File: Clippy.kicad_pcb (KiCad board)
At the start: 2 copper layers, 61.2 x 38.4 mm, 15 parts, among them J1 Conn_01x08, SW1 PEC11R-4215F-S0024, U1 tiny2040, U2 SN74LV1T34DBV

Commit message: Final touches?
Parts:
- added C2: 100nF, Capacitor_SMD:C_0402_1005Metric_Pad0.74x0.62mm_HandSolder, B.Cu at (150.3, 92.5)
- added C3: 100nF, Capacitor_SMD:C_0402_1005Metric_Pad0.74x0.62mm_HandSolder, B.Cu at (169.3, 92.4)
- moved D1 1.27 mm to (127.5, 83.7)
- moved D2 1.27 mm to (131.3, 83.7)
- moved D3 1.27 mm to (135.1, 83.7)
- moved D4 1.27 mm to (138.9, 83.7)
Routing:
- net +5V: track 124.9 -> 126.2 mm
- net Net-(D2-A): track 29.9 -> 30.4 mm
- net Net-(D3-A): track 49.7 -> 50.2 mm
- net Net-(D1-A): track 58.4 -> 58.9 mm
- net ROW1: track 19.6 -> 19.1 mm
- net Net-(D4-A): track 35.8 -> 36.4 mm
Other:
- board text added: "+3V3"
- board text added: "+5V"
- board text added: "GND"
- board text added: "GP26"
- board text added: "GP27"
- board text added: "GP28"
- board text added: "GP29"
- board text added: "GP7"

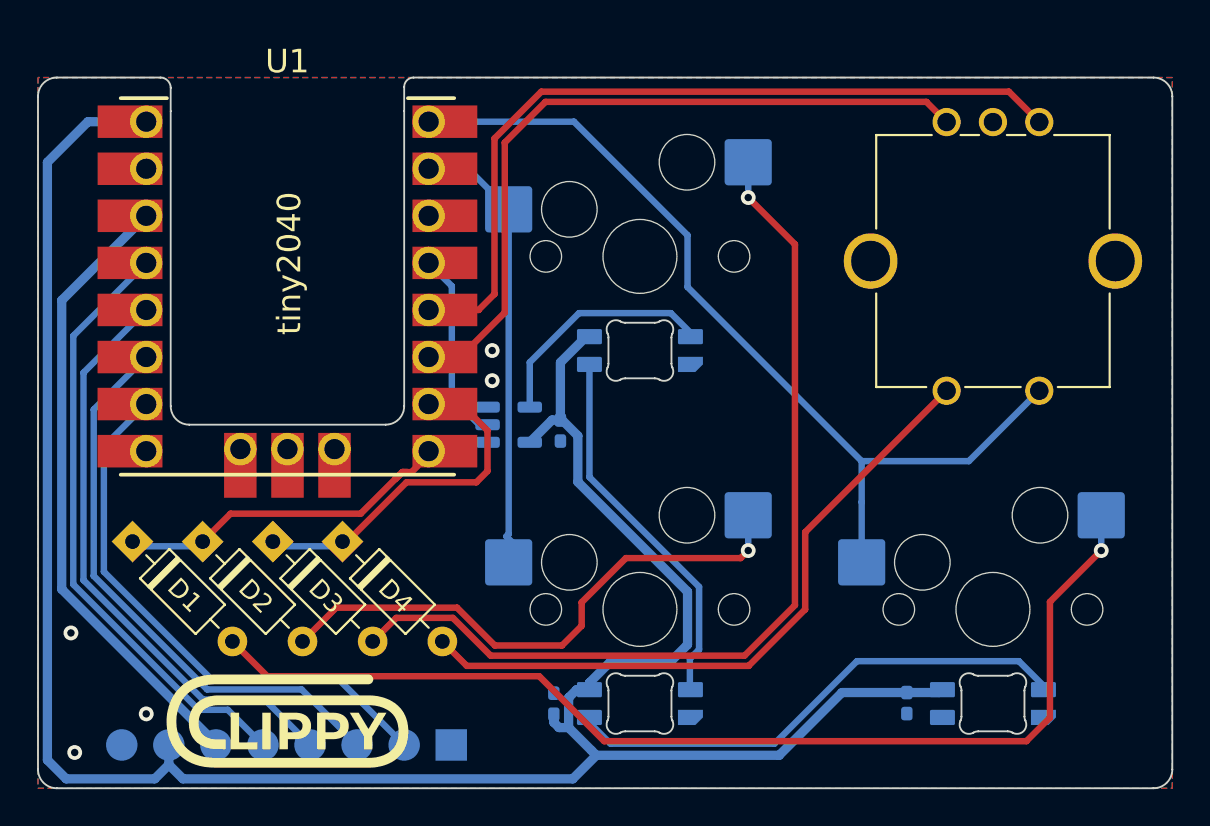
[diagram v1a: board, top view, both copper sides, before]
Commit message: oops. Actually add tooling holes
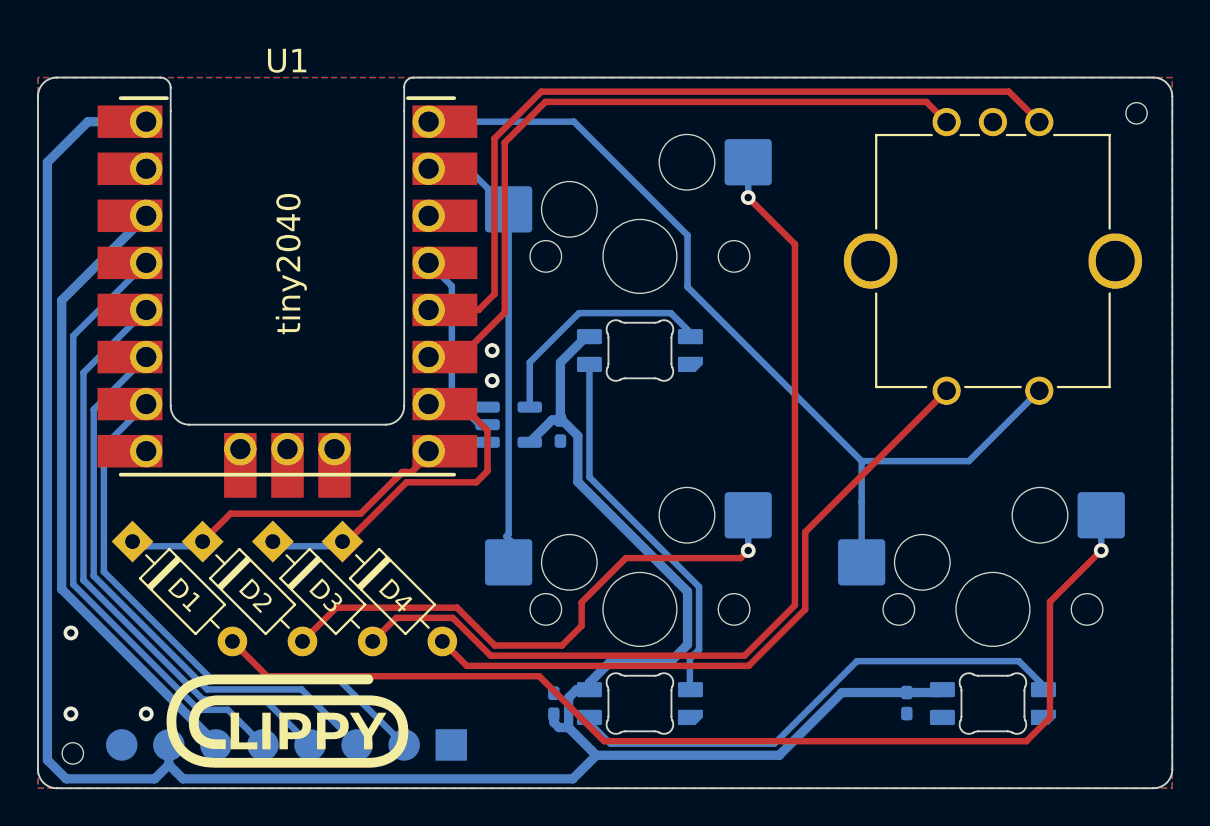
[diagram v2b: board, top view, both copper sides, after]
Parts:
- added REF**: MountingHole_1.152mm, MountingHole:MountingHole_1.152mm, F.Cu at (181.7, 60.6)
- added REF**: MountingHole_1.152mm, MountingHole:MountingHole_1.152mm, F.Cu at (124.3, 95.1)
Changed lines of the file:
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@@
       (net 5 "Net-(D3-A)") (pinfunction "ROW") (pintype "passive"))
+  )
+  (footprint "MountingHole:MountingHole_1.152mm" (layer "F.Cu")
+    (at 181.7116 60.6044)
+    (descr "Mounting Hole 2.1mm, no annular")
+    (tags "mounting hole 2.1mm no annular")
+    (attr exclude_from_pos_files exclude_from_bom)
+    (fp_text reference "REF**" (at 0 -3.2) (layer "F.SilkS") hide
+        (effects (font (size 1 1) (thickness 0.15)))
+    )
+    (fp_text value "MountingHole_1.152mm" (at 0 3.2) (layer "F.Fab")
+        (effects (font (size 1 1) (thickness 0.15)))
+    )
+    (fp_text user "${REFERENCE}" (at 0 0) (layer "F.Fab")
+        (effects (font (size 1 1) (thickness 0.15)))
+    )
+    (fp_circle (center 0 0) (end 1.25 0)
+      (stroke (width 0.15) (type solid)) (fill none) (layer "Cmts.User"))
+    (fp_circle (center 0 0) (end 1.5 0)
+      (stroke (width 0.05) (type solid)) (fill none) (layer "F.CrtYd"))
+    (pad "" np_thru_hole circle (at 0 0) (size 1.152 1.152) (drill 1.152) (layers "F&B.Cu" "*.Mask")
+      (solder_mask_margin 0.148))
   )
   (footprint "Diode_THT:D_DO-35_SOD27_P7.62mm_Horizontal" (layer "F.Cu")
@@
       (rotate (xyz 0 0 0))
     )
+  )
+  (footprint "MountingHole:MountingHole_1.152mm" (layer "F.Cu")
+    (at 124.3076 95.1484)
+    (descr "Mounting Hole 2.1mm, no annular")
+    (tags "mounting hole 2.1mm no annular")
+    (attr exclude_from_pos_files exclude_from_bom)
+    (fp_text reference "REF**" (at 0 -3.2) (layer "F.SilkS") hide
+        (effects (font (size 1 1) (thickness 0.15)))
+    )
+    (fp_text value "MountingHole_1.152mm" (at 0 3.2) (layer "F.Fab")
+        (effects (font (size 1 1) (thickness 0.15)))
+    )
+    (fp_text user "${REFERENCE}" (at 0 0) (layer "F.Fab")
+        (effects (font (size 1 1) (thickness 0.15)))
+    )
+    (fp_circle (center 0 0) (end 1.25 0)
+      (stroke (width 0.15) (type solid)) (fill none) (layer "Cmts.User"))
+    (fp_circle (center 0 0) (end 1.5 0)
+      (stroke (width 0.05) (type solid)) (fill none) (layer "F.CrtYd"))
+    (pad "" np_thru_hole circle (at 0 0) (size 1.152 1.152) (drill 1.152) (layers "*.Cu" "*.Mask")
+      (solder_mask_margin 0.148))
   )
   (footprint "Rotary_Encoder:RotaryEncoder_Bourns_Vertical_PEC12R-3xxxF-Sxxxx" (layer "F.Cu")
@@
     (fp_arc (start -1.699999 0.702844) (mid -1.712527 0.814069) (end -1.749484 0.919721)
       (stroke (width 0.1) (type solid)) (layer "Edge.Cuts"))
-    (fp_arc (start -1.046711 1.568299) (mid -1.638071 1.504035) (end -1.749484 0.919721)
+    (fp_arc (start -1.046711 1.568299) (mid -1.63807 1.504035) (end -1.749484 0.919721)
       (stroke (width 0.1) (type solid)) (layer "Edge.Cuts"))
     (fp_arc (start -1.046711 1.568299) (mid -0.925123 1.517377) (end -0.794453 1.5)
@@
     (fp_arc (start 1.749484 0.919721) (mid 1.638072 1.504036) (end 1.046711 1.5683)
       (stroke (width 0.1) (type solid)) (layer "Edge.Cuts"))
-    (fp_arc (start 1.749484 0.919721) (mid 1.712539 0.814068) (end 1.699999 0.702843)
+    (fp_arc (start 1.749484 0.919721) (mid 1.712534 0.814067) (end 1.699999 0.702843)
       (stroke (width 0.1) (type solid)) (layer "Edge.Cuts"))
     (fp_line (start -3.8 -1.999999) (end -3.8 2.000001)
@@
     (fp_arc (start -1.699999 0.702844) (mid -1.712527 0.814069) (end -1.749484 0.919721)
       (stroke (width 0.1) (type solid)) (layer "Edge.Cuts"))
-    (fp_arc (start -1.046711 1.568299) (mid -1.638071 1.504035) (end -1.749484 0.919721)
+    (fp_arc (start -1.046711 1.568299) (mid -1.63807 1.504035) (end -1.749484 0.919721)
       (stroke (width 0.1) (type solid)) (layer "Edge.Cuts"))
     (fp_arc (start -1.046711 1.568299) (mid -0.925123 1.517377) (end -0.794453 1.5)
@@
     (fp_arc (start 1.749484 0.919721) (mid 1.638072 1.504036) (end 1.046711 1.5683)
       (stroke (width 0.1) (type solid)) (layer "Edge.Cuts"))
-    (fp_arc (start 1.749484 0.919721) (mid 1.712539 0.814068) (end 1.699999 0.702843)
+    (fp_arc (start 1.749484 0.919721) (mid 1.712534 0.814067) (end 1.699999 0.702843)
       (stroke (width 0.1) (type solid)) (layer "Edge.Cuts"))
     (fp_line (start -3.8 -1.999999) (end -3.8 2.000001)
@@
     (fp_arc (start -1.699999 0.702844) (mid -1.712527 0.814069) (end -1.749484 0.919721)
       (stroke (width 0.1) (type solid)) (layer "Edge.Cuts"))
-    (fp_arc (start -1.046711 1.568299) (mid -1.638071 1.504035) (end -1.749484 0.919721)
+    (fp_arc (start -1.046711 1.568299) (mid -1.63807 1.504035) (end -1.749484 0.919721)
       (stroke (width 0.1) (type solid)) (layer "Edge.Cuts"))
     (fp_arc (start -1.046711 1.568299) (mid -0.925123 1.517377) (end -0.794453 1.5)
@@
     (fp_arc (start 1.749484 0.919721) (mid 1.638072 1.504036) (end 1.046711 1.5683)
       (stroke (width 0.1) (type solid)) (layer "Edge.Cuts"))
-    (fp_arc (start 1.749484 0.919721) (mid 1.712539 0.814068) (end 1.699999 0.702843)
+    (fp_arc (start 1.749484 0.919721) (mid 1.712534 0.814067) (end 1.699999 0.702843)
       (stroke (width 0.1) (type solid)) (layer "Edge.Cuts"))
     (fp_line (start -3.8 -1.999999) (end -3.8 2.000001)
@@
   (via (at 146.939 73.406) (size 0.8) (drill 0.4) (layers "F.Cu" "B.Cu") (free) (net 12))
   (via (at 128.27 93.0148) (size 0.8) (drill 0.4) (layers "F.Cu" "B.Cu") (free) (net 12))
-  (via (at 124.4092 95.0976) (size 0.8) (drill 0.4) (layers "F.Cu" "B.Cu") (free) (net 12))
+  (via (at 124.206 93.0148) (size 0.8) (drill 0.4) (layers "F.Cu" "B.Cu") (free) (net 12))
   (via (at 124.206 88.646) (size 0.8) (drill 0.4) (layers "F.Cu" "B.Cu") (free) (net 12))
   (segment (start 175.365187 90.17) (end 166.624 90.17) (width 0.35) (layer "B.Cu") (net 13))

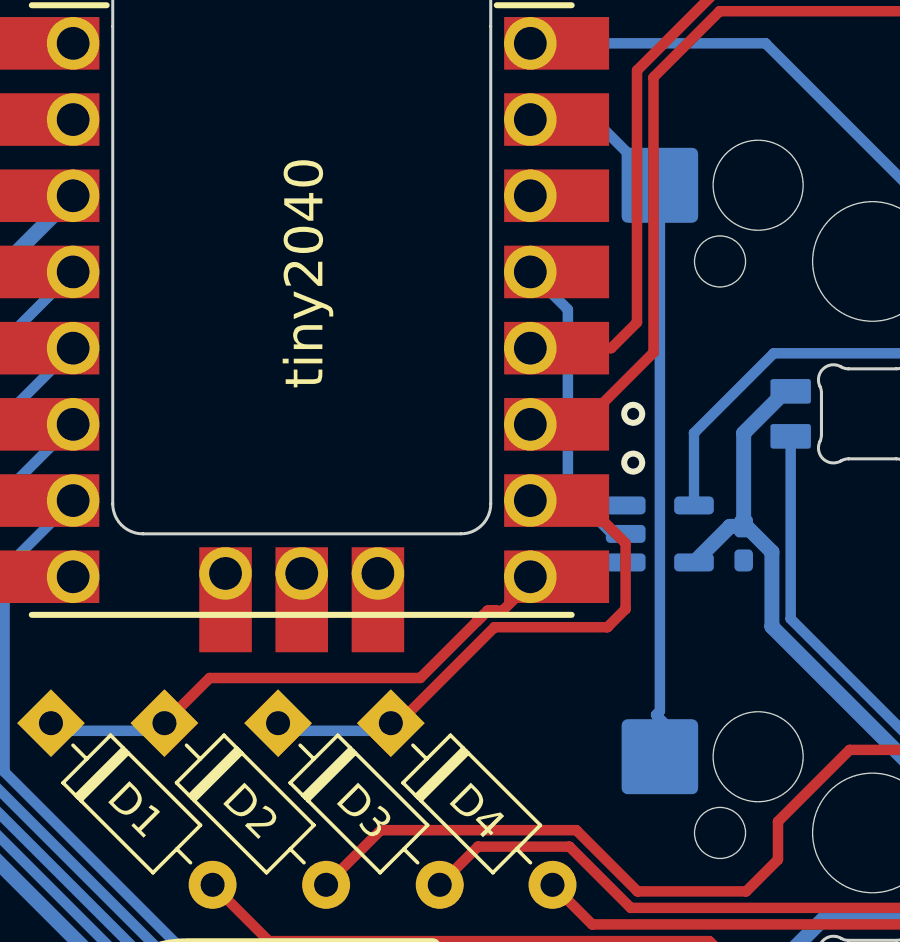
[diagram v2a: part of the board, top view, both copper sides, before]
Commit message: Fix DRC errors to a reasonable extent
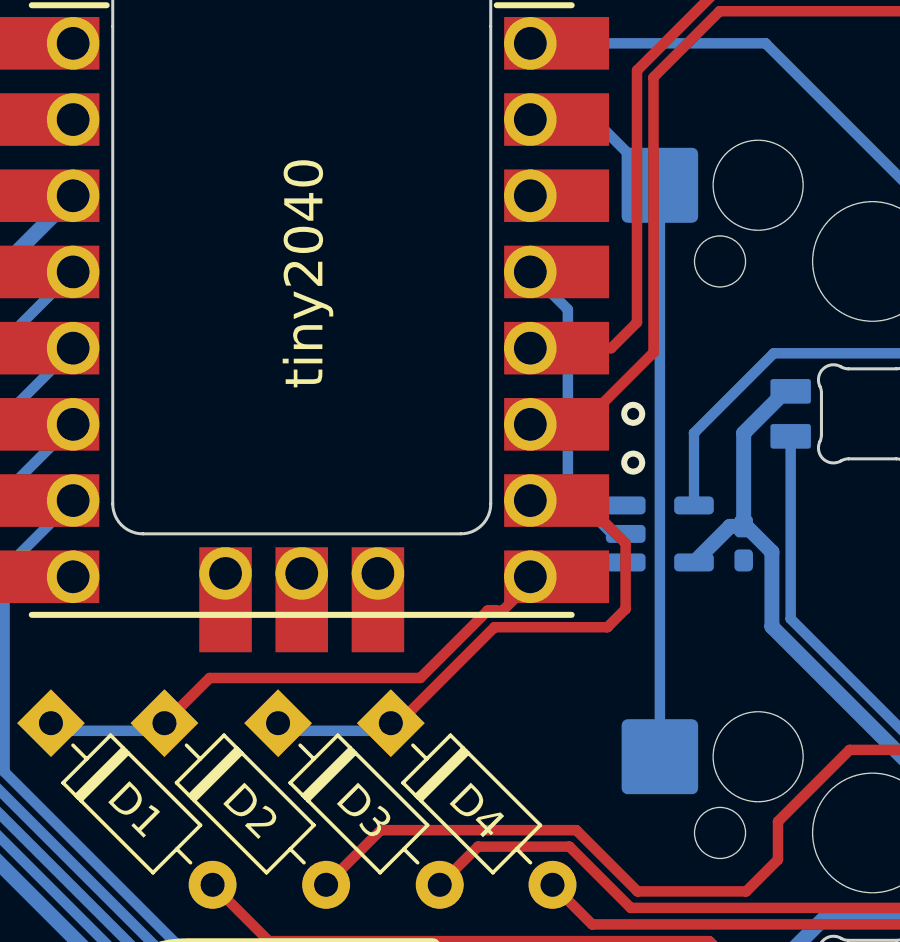
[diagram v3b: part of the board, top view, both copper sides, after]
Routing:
- net COL0: track 26.3 -> 24.3 mm
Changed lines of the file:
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@@
   )
   (segment (start 142.5868 79.968) (end 143.51 79.0448) (width 0.35) (layer "F.Cu") (net 1))
+  (segment (start 132.82018 82.210353) (end 139.843516 82.210353) (width 0.35) (layer "F.Cu") (net 1))
   (segment (start 143.51 79.0448) (end 143.51 78.83605) (width 0.35) (layer "F.Cu") (net 1))
+  (segment (start 139.843516 82.210353) (end 142.085869 79.968) (width 0.35) (layer "F.Cu") (net 1))
   (segment (start 142.092818 79.96105) (end 142.362488 79.96105) (width 0.35) (layer "F.Cu") (net 1))
-  (segment (start 139.843515 82.210353) (end 141.93335 80.120518) (width 0.35) (layer "F.Cu") (net 1))
-  (segment (start 132.82018 82.210353) (end 139.843515 82.210353) (width 0.35) (layer "F.Cu") (net 1))
-  (segment (start 141.710134 80.343734) (end 142.092818 79.96105) (width 0.35) (layer "F.Cu") (net 1))
+  (segment (start 131.313809 83.716724) (end 132.82018 82.210353) (width 0.35) (layer "F.Cu") (net 1))
   (segment (start 142.085869 79.968) (end 142.5868 79.968) (width 0.35) (layer "F.Cu") (net 1))
-  (segment (start 131.313809 83.716724) (end 132.82018 82.210353) (width 0.35) (layer "F.Cu") (net 1))
   (segment (start 127.530886 83.970724) (end 131.313809 83.970724) (width 0.35) (layer "B.Cu") (net 1))
   (segment (start 177.038 93.218) (end 175.768 94.488) (width 0.35) (layer "F.Cu") (net 2))
@@
   (segment (start 153.326 94.625) (end 152.188 93.487) (width 0.35) (layer "B.Cu") (net 13))
   (segment (start 152.188 93.487) (end 152.188 93.206) (width 0.35) (layer "B.Cu") (net 13))
-  (segment (start 147.828 84.836) (end 148.844 83.82) (width 0.35) (layer "B.Cu") (net 14))
-  (segment (start 148.463 84.201) (end 147.701 83.439) (width 0.35) (layer "B.Cu") (net 14))
-  (segment (start 147.828 83.312) (end 147.828 65.786) (width 0.35) (layer "B.Cu") (net 14))
-  (segment (start 147.701 83.439) (end 147.828 83.312) (width 0.35) (layer "B.Cu") (net 14))
   (segment (start 145.63805 63.59605) (end 143.51 63.59605) (width 0.35) (layer "B.Cu") (net 14))
-  (segment (start 147.828 84.836) (end 148.463 84.201) (width 0.35) (layer "B.Cu") (net 14))
   (segment (start 147.828 65.786) (end 145.63805 63.59605) (width 0.35) (layer "B.Cu") (net 14))
+  (segment (start 147.828 84.836) (end 147.828 65.786) (width 0.35) (layer "B.Cu") (net 14))
   (segment (start 143.51 61.05605) (end 151.35305 61.05605) (width 0.35) (layer "B.Cu") (net 15))
   (segment (start 166.878 79.375) (end 166.878 81.5848) (width 0.35) (layer "B.Cu") (net 15))

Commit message: finishing touches
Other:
- board text added: "Clippy Rev. 1 • April 2023"

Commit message: finishing touches 2 electric boogaloo
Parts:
- removed the REF** at (181.7, 60.6)
- removed the REF** at (124.3, 95.1)
- added REF**: MountingHole_1.152mm, MountingHole:MountingHole_1.152mm, F.Cu at (124.3, 95.1)
- added REF**: MountingHole_1.152mm, MountingHole:MountingHole_1.152mm, F.Cu at (181.7, 60.6)
- C1, C2, C3: footprint Capacitor_SMD:C_0402_1005Metric_Pad0.74x0.62mm_HandSolder -> Capacitor_SMD:C_0805_2012Metric_Pad1.18x1.45mm_HandSolder
- moved C1 1.42 mm to (151.9, 78.4), turned to 180 degrees
- moved C2 0.41 mm to (149.9, 92.5)
- moved C3 0.41 mm to (168.9, 92.4)
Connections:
- J1 pad 1: GP7 -> GP2
- U1 pad 14: unconnected-(U1-GP2-Pad14) -> GP2
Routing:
- net GP2: track 0.00 -> 35.5 mm, vias 0 -> 2
- net +5V: track 126.2 -> 118.0 mm
- net COL0: track 24.3 -> 25.8 mm
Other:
- board text added: "Clipboard Rev. 1 • April 2023"
- board text added: "EXPANSION"
- board text added: "GP2"
- board text added: "SCL"
- board text added: "SDA"
- board text removed: "Clippy Rev. 1 • April 2023"
- board text removed: "GP7"
